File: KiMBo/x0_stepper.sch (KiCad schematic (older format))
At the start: 25 parts, among them U15 TMC2130

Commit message: More stepper motor driver progress
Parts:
- renumbered R120 to R122, R121 to R123, R122 to R124, R123 to R125, R124 to R126, R125 to R127, R126 to R128, R127 to R129
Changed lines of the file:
@@
 $Descr A3 16535 11693
 encoding utf-8
-Sheet 17 25
+Sheet 15 25
 Title ""
 Date ""
@@
 $EndComp
 $Comp
-L R R127
+L R R129
 U 1 1 58C092F2
 P 10750 6700
-F 0 "R127" H 10700 6650 50  0000 R CNN
+F 0 "R129" H 10700 6650 50  0000 R CNN
 F 1 "220mΩ" H 10700 6750 50  0000 R CNN
 F 2 "Resistors_SMD:R_0805" V 10680 6700 50  0001 C CNN
@@
 $EndComp
 $Comp
-L R R126
+L R R128
 U 1 1 58C092F9
 P 9950 6700
-F 0 "R126" H 9900 6650 50  0000 R CNN
+F 0 "R128" H 9900 6650 50  0000 R CNN
 F 1 "220mΩ" H 9900 6750 50  0000 R CNN
 F 2 "Resistors_SMD:R_0805" V 9880 6700 50  0001 C CNN
@@
 NoConn ~ 7700 5600
 $Comp
-L R R123
+L R R125
 U 1 1 5BA7E147
 P 7300 3750
-F 0 "R123" V 7200 3750 50  0000 C CNN
+F 0 "R125" V 7200 3750 50  0000 C CNN
 F 1 "2.2Ω" V 7300 3750 50  0000 C CNN
 F 2 "Resistors_SMD:R_0603" V 7230 3750 50  0001 C CNN
@@
 X0_FAULT
 $Comp
-L R R121
+L R R123
 U 1 1 58C09331
 P 6050 4250
-F 0 "R121" H 6119 4296 50  0000 L CNN
+F 0 "R123" H 6119 4296 50  0000 L CNN
 F 1 "4.7kΩ" H 6119 4205 50  0000 L CNN
 F 2 "Resistors_SMD:R_0603" V 5980 4250 50  0001 C CNN
@@
 5VOUT
 $Comp
-L R R124
+L R R126
 U 1 1 5BA7E14D
 P 9250 6700
-F 0 "R124" H 9319 6746 50  0000 L CNN
+F 0 "R126" H 9319 6746 50  0000 L CNN
 F 1 "5.23kΩ" H 9319 6655 50  0000 L CNN
 F 2 "Resistors_SMD:R_0603" V 9180 6700 50  0001 C CNN
@@
 5VOUT
 $Comp
-L R R125
+L R R127
 U 1 1 5BA7E14E
 P 9450 6900
-F 0 "R125" V 9250 6900 50  0000 C CNN
+F 0 "R127" V 9250 6900 50  0000 C CNN
 F 1 "4.75kΩ" V 9350 6900 50  0000 C CNN
 F 2 "Resistors_SMD:R_0603" V 9380 6900 50  0001 C CNN
@@
 $EndComp
 $Comp
-L R R122
+L R R124
 U 1 1 58C09353
 P 6400 4250
-F 0 "R122" H 6469 4296 50  0000 L CNN
+F 0 "R124" H 6469 4296 50  0000 L CNN
 F 1 "4.7kΩ" H 6469 4205 50  0000 L CNN
 F 2 "Resistors_SMD:R_0603" V 6330 4250 50  0001 C CNN
@@
 	9150 6000 9150 5950
 $Comp
-L R R120
+L R R122
 U 1 1 5BA7E158
 P 5700 4250
-F 0 "R120" H 5769 4296 50  0000 L CNN
+F 0 "R122" H 5769 4296 50  0000 L CNN
 F 1 "4.7kΩ" H 5769 4205 50  0000 L CNN
 F 2 "Resistors_SMD:R_0603" V 5630 4250 50  0001 C CNN

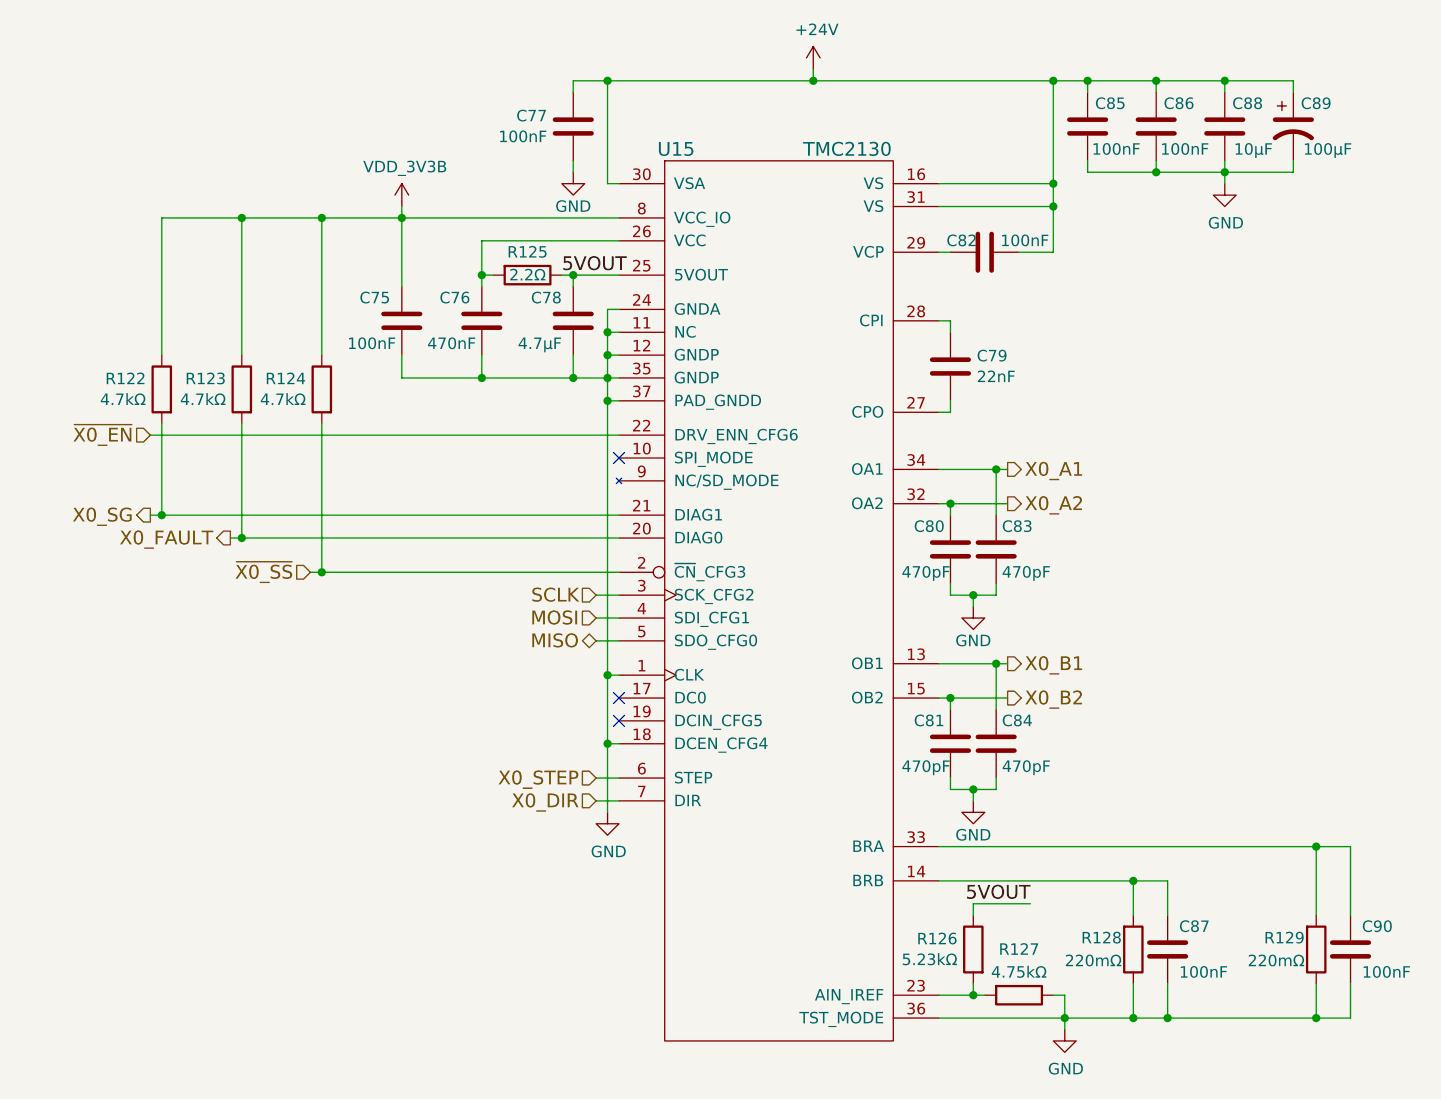
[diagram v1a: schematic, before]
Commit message: Daisy chain the SPI stepper motor driver interface, continue work on the E-heater layout
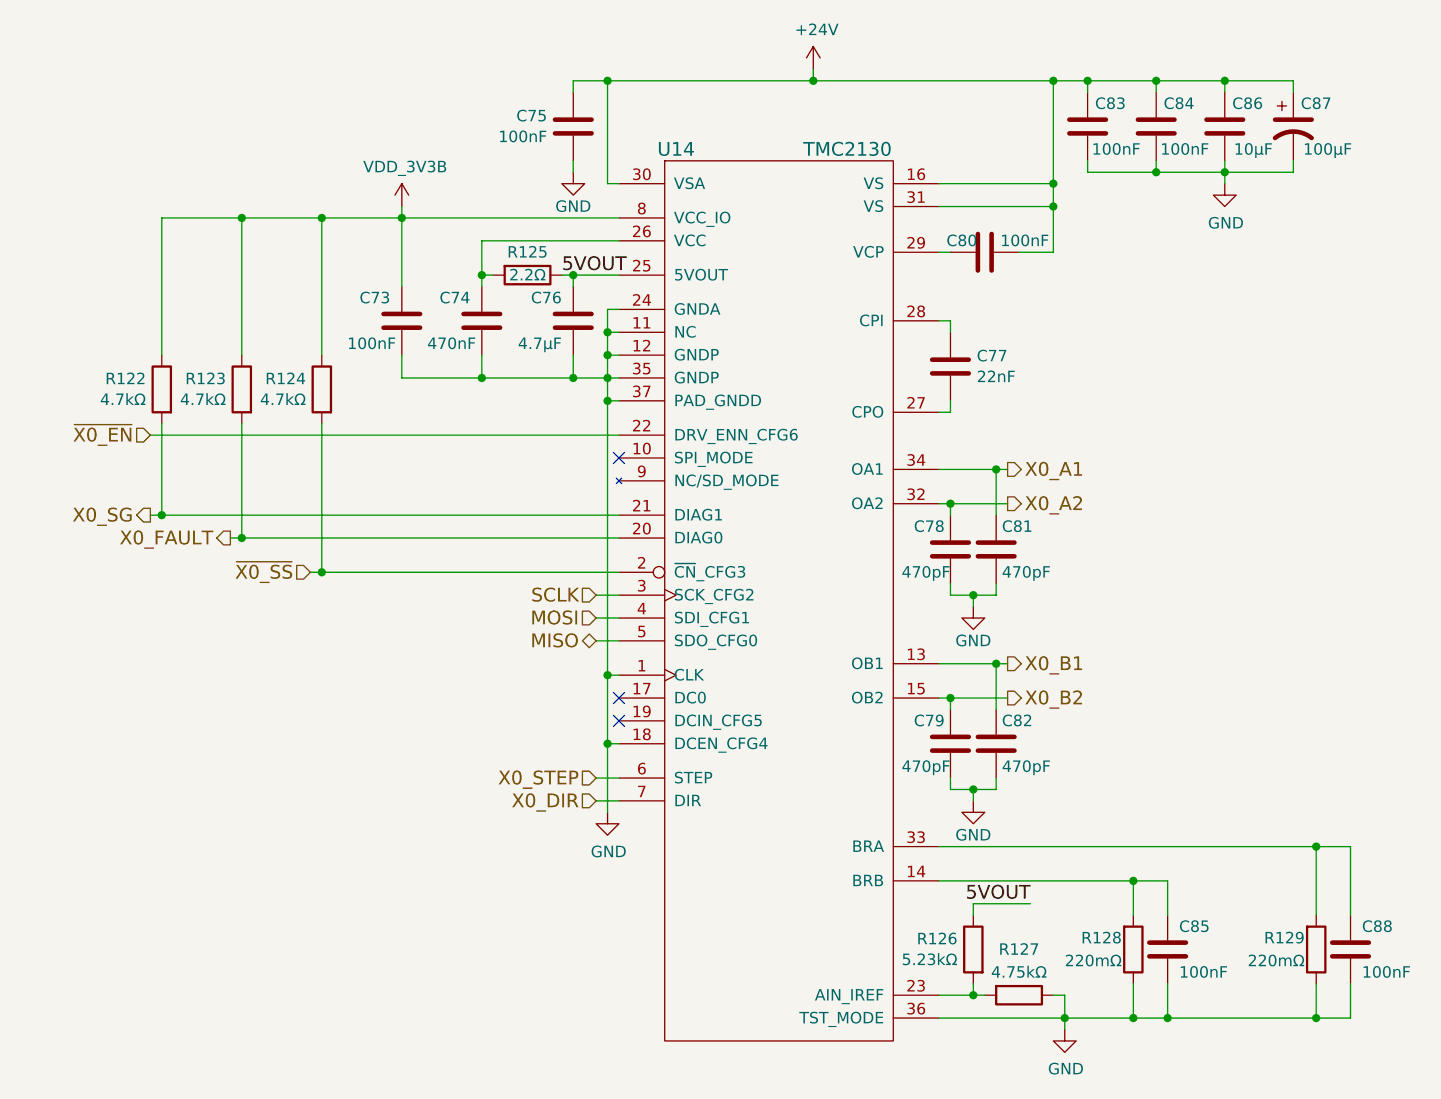
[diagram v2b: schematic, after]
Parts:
- renumbered C75 to C73, C76 to C74, C77 to C75, C78 to C76, C79 to C77, C80 to C78, C81 to C79, C82 to C80, C83 to C81, C84 to C82, C85 to C83, C86 to C84, C87 to C85, C88 to C86, C89 to C87, C90 to C88, U15 to U14
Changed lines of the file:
@@
 X0_SG
 $Comp
-L C C77
+L C C75
 U 1 1 5BA7E13B
 P 7500 3100
-F 0 "C77" H 7386 3054 50  0000 R CNN
+F 0 "C75" H 7386 3054 50  0000 R CNN
 F 1 "100nF" H 7386 3145 50  0000 R CNN
 F 2 "Capacitors_SMD:C_0603" H 7538 2950 50  0001 C CNN
@@
 $EndComp
 $Comp
-L C C82
+L C C80
 U 1 1 5BA7E13C
 P 9300 3650
-F 0 "C82" V 9250 3550 50  0000 C CNN
+F 0 "C80" V 9250 3550 50  0000 C CNN
 F 1 "100nF" V 9250 3825 50  0000 C CNN
 F 2 "Capacitors_SMD:C_0603" H 9338 3500 50  0001 C CNN
@@
 $EndComp
 $Comp
-L CP1 C89
+L CP1 C87
 U 1 1 58C092C4
 P 10650 3100
-F 0 "C89" H 10750 3200 50  0000 C CNN
+F 0 "C87" H 10750 3200 50  0000 C CNN
 F 1 "100μF" H 10800 3000 50  0000 C CNN
 F 2 "Capacitors_SMD:c_elec_8x10" H 10650 3100 50  0001 C CNN
@@
 $EndComp
 $Comp
-L C C85
+L C C83
 U 1 1 58C092CB
 P 9750 3100
-F 0 "C85" H 9650 3200 50  0000 C CNN
+F 0 "C83" H 9650 3200 50  0000 C CNN
 F 1 "100nF" H 9625 3000 50  0000 C CNN
 F 2 "Capacitors_SMD:C_0603" H 9788 2950 50  0001 C CNN
@@
 $EndComp
 $Comp
-L GND #PWR0177
+L GND #PWR157
 U 1 1 58C092D2
 P 7500 3300
-F 0 "#PWR0177" H 7500 3050 50  0001 C CNN
+F 0 "#PWR157" H 7500 3050 50  0001 C CNN
 F 1 "GND" H 7500 3150 50  0000 C CNN
 F 2 "" H 7500 3300 50  0000 C CNN
@@
 $EndComp
 $Comp
-L C C86
+L C C84
 U 1 1 5BA7E140
 P 10050 3100
-F 0 "C86" H 9950 3200 50  0000 C CNN
+F 0 "C84" H 9950 3200 50  0000 C CNN
 F 1 "100nF" H 9925 3000 50  0000 C CNN
 F 2 "Capacitors_SMD:C_0603" H 10088 2950 50  0001 C CNN
@@
 $EndComp
 $Comp
-L GND #PWR0178
+L GND #PWR163
 U 1 1 5BA7E141
 P 10350 3350
-F 0 "#PWR0178" H 10350 3100 50  0001 C CNN
+F 0 "#PWR163" H 10350 3100 50  0001 C CNN
 F 1 "GND" H 10355 3177 50  0000 C CNN
 F 2 "" H 10350 3350 50  0000 C CNN
@@
 $EndComp
 $Comp
-L +24V #PWR0179
+L +24V #PWR159
 U 1 1 58C092E5
 P 8550 2850
-F 0 "#PWR0179" H 8550 2700 50  0001 C CNN
+F 0 "#PWR159" H 8550 2700 50  0001 C CNN
 F 1 "+24V" H 8565 3023 50  0000 C CNN
 F 2 "" H 8550 2850 50  0000 C CNN
@@
 $EndComp
 $Comp
-L C C79
+L C C77
 U 1 1 58C092EB
 P 9150 4150
-F 0 "C79" H 9265 4196 50  0000 L CNN
+F 0 "C77" H 9265 4196 50  0000 L CNN
 F 1 "22nF" H 9265 4105 50  0000 L CNN
 F 2 "Capacitors_SMD:C_0603" H 9188 4000 50  0001 C CNN
@@
 $EndComp
 $Comp
-L GND #PWR0180
+L GND #PWR162
 U 1 1 5BA7E146
 P 9650 7050
-F 0 "#PWR0180" H 9650 6800 50  0001 C CNN
+F 0 "#PWR162" H 9650 6800 50  0001 C CNN
 F 1 "GND" H 9655 6877 50  0000 C CNN
 F 2 "" H 9650 7050 50  0000 C CNN
@@
 $EndComp
 $Comp
-L C C76
+L C C74
 U 1 1 5BA7E148
 P 7100 3950
-F 0 "C76" H 7150 4050 50  0000 L CNN
+F 0 "C74" H 7150 4050 50  0000 L CNN
 F 1 "470nF" H 7125 3850 50  0000 L CNN
 F 2 "Capacitors_SMD:C_0603" H 7138 3800 50  0001 C CNN
@@
 NoConn ~ 7700 5700
 $Comp
-L GND #PWR0181
+L GND #PWR158
 U 1 1 5BA7E149
 P 7650 6100
-F 0 "#PWR0181" H 7650 5850 50  0001 C CNN
+F 0 "#PWR158" H 7650 5850 50  0001 C CNN
 F 1 "GND" H 7655 5927 50  0000 C CNN
 F 2 "" H 7650 6100 50  0000 C CNN
@@
 $EndComp
 $Comp
-L C C87
+L C C85
 U 1 1 5BA7E14A
 P 10100 6700
-F 0 "C87" H 10150 6800 50  0000 L CNN
+F 0 "C85" H 10150 6800 50  0000 L CNN
 F 1 "100nF" H 10150 6600 50  0000 L CNN
 F 2 "Capacitors_SMD:C_0603" H 10138 6550 50  0001 C CNN
@@
 NoConn ~ 7700 4550
 $Comp
-L C C78
+L C C76
 U 1 1 5BA7E14C
 P 7500 3950
-F 0 "C78" H 7550 4050 50  0000 L CNN
+F 0 "C76" H 7550 4050 50  0000 L CNN
 F 1 "4.7μF" H 7550 3850 50  0000 L CNN
 F 2 "Capacitors_SMD:C_0603" H 7538 3800 50  0001 C CNN
@@
 $EndComp
 $Comp
-L C C90
+L C C88
 U 1 1 58C0935A
 P 10900 6700
-F 0 "C90" H 10950 6800 50  0000 L CNN
+F 0 "C88" H 10950 6800 50  0000 L CNN
 F 1 "100nF" H 10950 6600 50  0000 L CNN
 F 2 "Capacitors_SMD:C_0603" H 10938 6550 50  0001 C CNN
@@
 $EndComp
 $Comp
-L C C80
+L C C78
 U 1 1 58C09363
 P 9150 4950
-F 0 "C80" H 9175 5050 50  0000 L CNN
+F 0 "C78" H 9175 5050 50  0000 L CNN
 F 1 "470pF" H 9150 4850 50  0000 L CNN
 F 2 "Capacitors_SMD:C_0603" H 9188 4800 50  0001 C CNN
@@
 $EndComp
 $Comp
-L GND #PWR0182
+L GND #PWR160
 U 1 1 58C0936A
 P 9250 5200
-F 0 "#PWR0182" H 9250 4950 50  0001 C CNN
+F 0 "#PWR160" H 9250 4950 50  0001 C CNN
 F 1 "GND" H 9250 5050 50  0000 C CNN
 F 2 "" H 9250 5200 50  0000 C CNN
@@
 $EndComp
 $Comp
-L C C83
+L C C81
 U 1 1 58C09370
 P 9350 4950
-F 0 "C83" H 9375 5050 50  0000 L CNN
+F 0 "C81" H 9375 5050 50  0000 L CNN
 F 1 "470pF" H 9375 4850 50  0000 L CNN
 F 2 "Capacitors_SMD:C_0603" H 9388 4800 50  0001 C CNN
@@
 $EndComp
 $Comp
-L C C81
+L C C79
 U 1 1 5BA7E154
 P 9150 5800
-F 0 "C81" H 9175 5900 50  0000 L CNN
+F 0 "C79" H 9175 5900 50  0000 L CNN
 F 1 "470pF" H 9150 5700 50  0000 L CNN
 F 2 "Capacitors_SMD:C_0603" H 9188 5650 50  0001 C CNN
@@
 $EndComp
 $Comp
-L GND #PWR0183
+L GND #PWR161
 U 1 1 58C0937E
 P 9250 6050
-F 0 "#PWR0183" H 9250 5800 50  0001 C CNN
+F 0 "#PWR161" H 9250 5800 50  0001 C CNN
 F 1 "GND" H 9250 5900 50  0000 C CNN
 F 2 "" H 9250 6050 50  0000 C CNN
@@
 $EndComp
 $Comp
-L C C84
+L C C82
 U 1 1 58C09384
 P 9350 5800
-F 0 "C84" H 9375 5900 50  0000 L CNN
+F 0 "C82" H 9375 5900 50  0000 L CNN
 F 1 "470pF" H 9375 5700 50  0000 L CNN
 F 2 "Capacitors_SMD:C_0603" H 9388 5650 50  0001 C CNN
@@
 $EndComp
 $Comp
-L TMC2130 U15
+L TMC2130 U14
 U 1 1 58C0938B
 P 8400 4700
-F 0 "U15" H 7950 6200 60  0000 C CNN
+F 0 "U14" H 7950 6200 60  0000 C CNN
 F 1 "TMC2130" H 8700 6200 60  0000 C CNN
 F 2 "KiMBo:QFN36_5X6" H 8400 5000 60  0001 C CNN
@@
 Connection ~ 6050 3500
 $Comp
-L C C88
+L C C86
 U 1 1 5BA7E159
 P 10350 3100
-F 0 "C88" H 10250 3200 50  0000 C CNN
+F 0 "C86" H 10250 3200 50  0000 C CNN
 F 1 "10μF" H 10225 3000 50  0000 C CNN
 F 2 "Capacitors_SMD:C_0805" H 10388 2950 50  0001 C CNN
@@
 	5700 3500 7700 3500
 $Comp
-L VDD_3V3B #PWR0184
+L VDD_3V3B #PWR156
 U 1 1 5A2FF856
 P 6750 3450
-F 0 "#PWR0184" H 6750 3300 50  0001 C CNN
+F 0 "#PWR156" H 6750 3300 50  0001 C CNN
 F 1 "VDD_3V3B" H 6765 3623 50  0000 C CNN
 F 2 "" H 6750 3450 50  0000 C CNN
@@
 $EndComp
 $Comp
-L C C75
+L C C73
 U 1 1 5A89853C
 P 6750 3950
-F 0 "C75" H 6800 4050 50  0000 L CNN
+F 0 "C73" H 6800 4050 50  0000 L CNN
 F 1 "100nF" H 6775 3850 50  0000 L CNN
 F 2 "Capacitors_SMD:C_0603" H 6788 3800 50  0001 C CNN
